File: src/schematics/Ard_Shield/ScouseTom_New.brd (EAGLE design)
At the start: 129.7 x 53.7 mm, 64 parts, among them IC1 LM317MBDT, IC2 AD5280, J1 STIM OUT, J4 Stim out Brd, Q2 FDN304P, Q3 FDV303N, T1 BC817, U1 ADM3202ARUZ, U3 ADUM5402ARWZ, U4 ADUM1410ARWZ, U5 ADUM5000ARWZ, U7 ADUM1410ARWZ, X1 IND DSUB, X2 SW DSUB, X3 CS DSUB

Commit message: gerber files and ignoring eagle backups
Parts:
- moved JP1 1.50 mm to (2.21, 38.1)
- moved J1 0.50 mm to (99.9, 16.6)
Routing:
- net GND_ISO_RS232: track 101.7 -> 99.7 mm, vias 9 -> 20
- net CS_EXTRA_ISO: track 32.9 -> 31.4 mm
- net STIM_OUT: track 23.5 -> 24.0 mm
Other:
- board text added: "???"
- board text added: "BONUS PINS"
- board text added: "CS Extra"
- board text added: "PMRK"
- board text added: "Tst1"
- board text added: "Tst2"
- board text added: "UCL EIT SCOUSETOM V2.5"
- board text removed: "PMARK"
- board text removed: "UCL EIT SCOUSETOM V2"

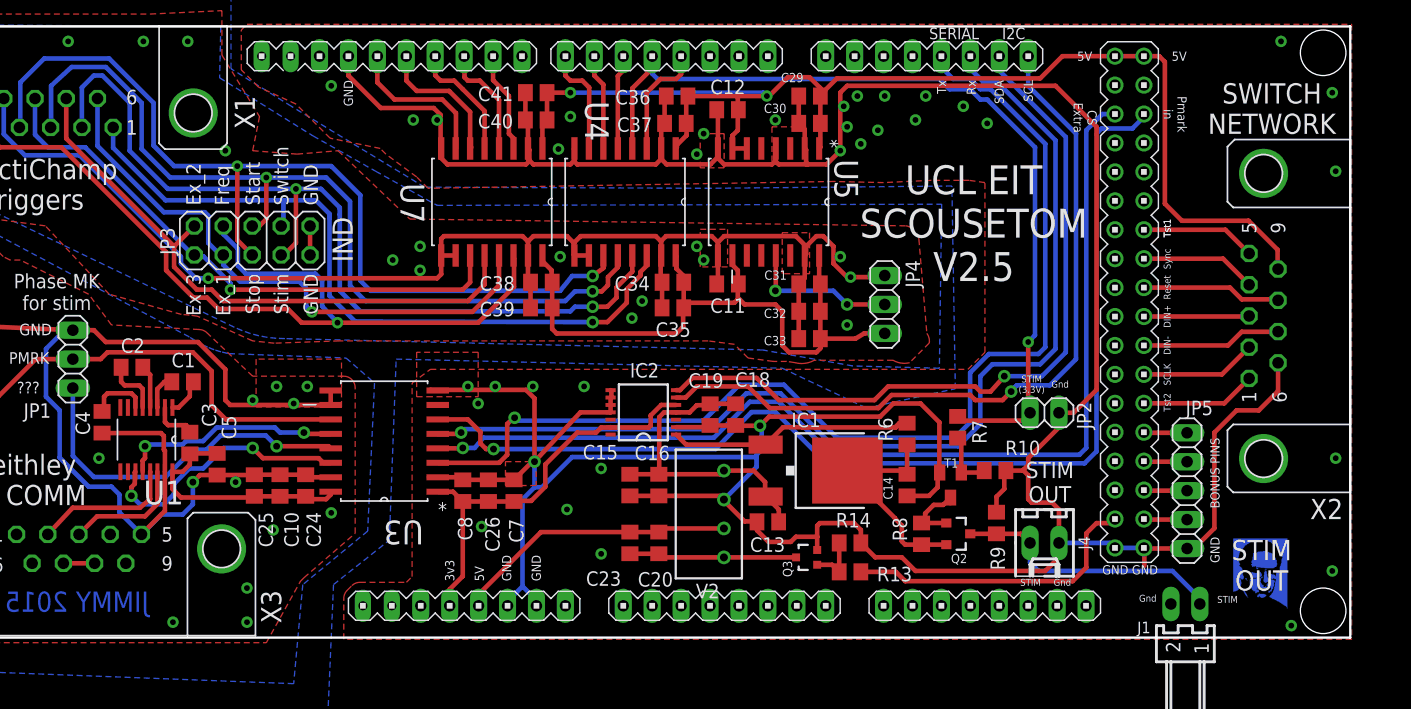
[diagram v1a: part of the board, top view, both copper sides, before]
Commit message: Final version sent to PCBTrain with BOM and P&P
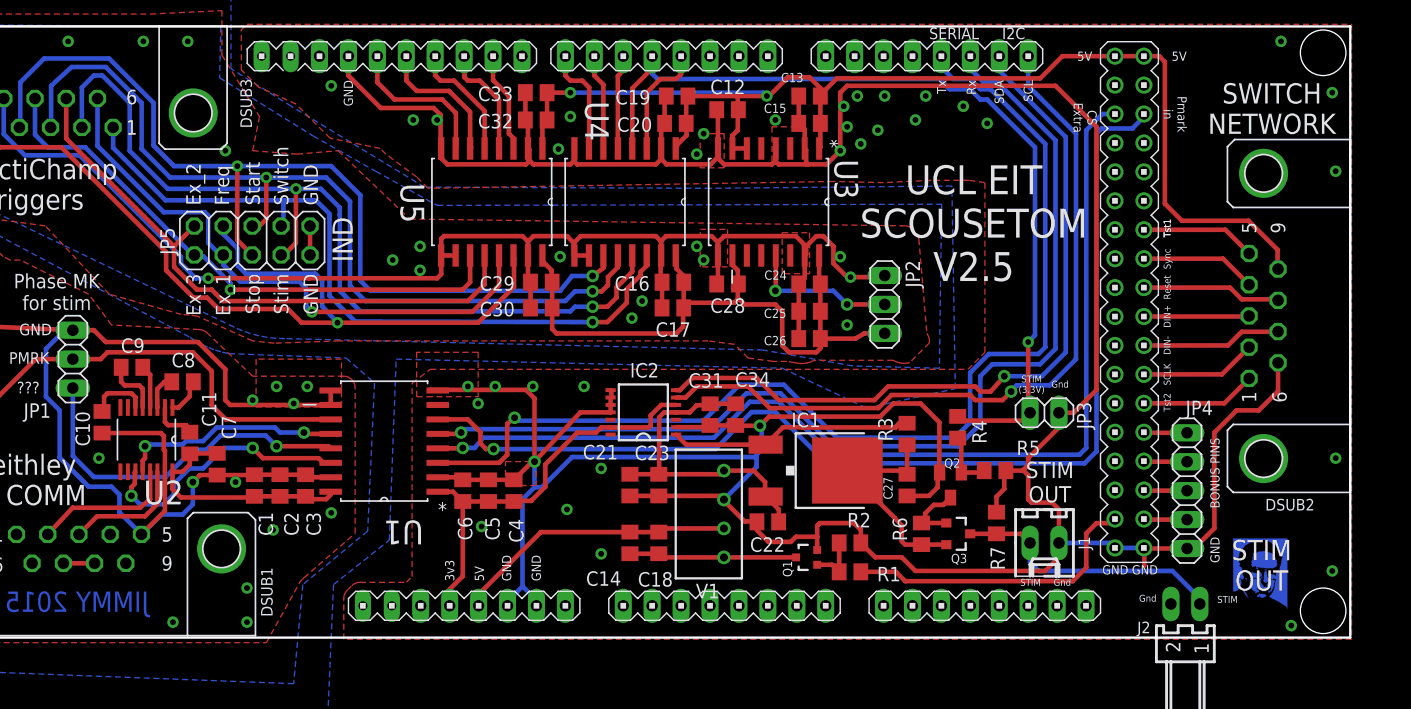
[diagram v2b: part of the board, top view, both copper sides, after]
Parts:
- removed C36, C38, C40: .1uF, resistor:C0805
- removed C37, C39, C41: 1uF, resistor:C0805
- removed J4: Stim out Brd, con-molex:6410-02
- removed R8: 5K1, resistor:R0805
- removed R9: 3k, resistor:R0805
- removed T1: BC817, transistor-npn:SOT23-BEC
- removed U7: ADUM1410ARWZ, ADI-Phase-2:SOIC127P1032X265-16N
- added C21, C28, C6: 10uF, resistor:C0805
- added C22, C9: 0.1uF, resistor:C0805
- added C27: 1uF, resistor:C0805
- added J2: STIM OUT, con-molex:7395-02
- added Q1: FDV303N, SparkFun-DiscreteSemi:SOT323
- added R3: 470, resistor:R0805
- added R4: 33k, resistor:R0805
- added U2: ADM3202ARUZ, Analog Devices_By_element14_Batch_1:SOP65P640X120-16N
- C1, C4: value 0.1uF -> 10nF
- C10, C34: value .1uF -> 0.1uF
- C11, C23, C8: value 10uF -> 0.1uF
- C13, C16, C2, C5: value 0.1uF -> .1uF
- C14: value 1uF -> 10uF
- C19: value 10uF -> .1uF
- C20: value 0.1uF -> 1uF
- C25: value 10nF -> .1uF
- C26: value .1uF -> 10nF
- C3: value 0.1uF -> 10uF
- C30: value 10uF -> 1uF
- C33: value 10nF -> 1uF
- C7: value 10nF -> 0.1uF
- J1: value STIM OUT -> Stim out Brd; device con-molex:7395-02 -> con-molex:6410-02
- JP2: value Ext Stim -> V_TRIG_SELECT; device pinhead:1X02 -> pinhead:1X03
- JP3: value IND_BK -> Ext Stim; device pinhead:2X05 -> pinhead:1X02
- JP4: value V_TRIG_SELECT -> BONUS_PINOUT; device pinhead:1X03 -> pinhead:1X05
- JP5: value BONUS_PINOUT -> IND_BK; device pinhead:1X05 -> pinhead:2X05
- Q2: value FDN304P -> BC817; device SparkFun-DiscreteSemi:SOT23-3 -> transistor-npn:SOT23-BEC
- Q3: value FDV303N -> FDN304P; device SparkFun-DiscreteSemi:SOT323 -> SparkFun-DiscreteSemi:SOT23-3
- R6: value 470 -> 5K1
- R7: value 33k -> 3k
- U1: value ADM3202ARUZ -> ADUM5402ARWZ; device Analog Devices_By_element14_Batch_1:SOP65P640X120-16N -> Analog Devices_By_element14_Batch_1:SOIC127P1032X265-16N
- U3: value ADUM5402ARWZ -> ADUM5000ARWZ
- U5: value ADUM5000ARWZ -> ADUM1410ARWZ; device Analog Devices_By_element14_Batch_1:SOIC127P1032X265-16N -> ADI-Phase-2:SOIC127P1032X265-16N
- moved JP5 85.0 mm to (18.0, 48.5), turned to 0 degrees
- moved JP3 71.2 mm to (87.5, 33.4)
- moved C25 51.1 mm to (66.9, 42.3), turned to 180 degrees
- moved C11 49.2 mm to (12.5, 30.7), turned to 90 degrees
- moved C24 47.7 mm to (66.9, 44.7), turned to 180 degrees
- moved U3 39.8 mm to (63.3, 51.9), turned to 270 degrees
- moved C13 37.6 mm to (66.9, 61.2), turned to 180 degrees
- moved C20 36.9 mm to (55.1, 58.8), turned to 180 degrees
- moved C4 36.7 mm to (41.0, 26.6), turned to 90 degrees
- moved C15 35.5 mm to (66.9, 58.8), turned to 180 degrees
- moved C33 32.3 mm to (42.9, 61.5)
- moved C26 31.2 mm to (66.9, 39.9), turned to 180 degrees
- moved JP4 31.2 mm to (100.0, 26.6)
- moved C32 29.3 mm to (42.9, 59.1)
- moved C29 28.7 mm to (43.4, 44.9)
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- renumbered C35 to C17, DIN8 to DIN1, DUE to ARD1, R10 to R5, R13 to R1, R14 to R2, V2 to V1, X1 to DSUB3, X2 to DSUB2, X3 to DSUB1
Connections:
- net +3V3: now also C4.1, C5.1, C6.1, U1.1; no longer C26.1, C7.1, C8.1, U3.1
- net +5V: now also C13.1, C15.1, C19.1, C20.1, C32.1, C33.1, U3.1, U3.6, U3.7; no longer C29.1, C30.1, C36.1, C37.1, C40.1, C41.1, U5.6, U5.7, U7.1
- net 5V_SIDE: now also C14.1, C18.2; no longer C20.2, C23.1
- net BONUS_1: now also JP4.1; no longer JP5.1
- net BONUS_2: now also JP4.2; no longer JP5.2
- net BONUS_3: now also JP4.3; no longer JP5.3
- net BONUS_4: now also JP4.4; no longer JP5.4
- net CS_EXTRA: now also U1.4; no longer U3.4
- net CS_EXTRA_ISO: now also U1.13; no longer U3.13
- net CS_PMARK: now also U1.6; no longer U3.6
- net CS_PMARK_ISO: now also U1.11; no longer U3.11
- net GND: now also C13.2, C20.2, C21.2, C22.1, C23.1, C27.1, C31.2, C32.2, C33.2, C34.1, C4.2, C5.2, C6.2, J2.2, JP3.2, JP4.5, Q1.2, Q2.E, R7.1, U1.2, U1.8, U3.3, U3.4; no longer C13.1, C14.1, C16.1, C18.1, C26.2, C29.2, C30.2, C36.2, C37.2, C40.2, C41.2, C7.2, C8.2, J4.2, JP2.2, JP5.5, Q3.2, R9.1, T1.E, U5.3, U5.4, U7.2, U7.8
- net GND_ISO_RS232: now also C1.2, C2.2, C3.2, C7.2, U1.10, U1.9, U2.15; no longer C24.2, C25.2, C4.2, C5.2, U3.10, U3.15, U3.9
- net GND_ISO_TRIG: now also C16.2, C24.2, C25.2, C26.2, C28.2, C29.2, C30.2, JP2.1, JP5.10, JP5.9, U3.11, U3.12, U3.14, U3.15, U3.9, U5.10; no longer C11.2, C31.2, C32.2, C33.2, C34.2, C38.2, C39.2, JP3.10, JP3.9, JP4.1, U5.11, U5.12, U5.14, U7.10, U7.15, U7.9
- net IND_EX_1: now also U5.4; no longer U7.4
- net IND_EX_1_ISO: now also JP5.3, U5.13; no longer JP3.3, U7.13
- net IND_EX_2: now also U5.5; no longer U7.5
- net IND_EX_2_ISO: now also JP5.2, U5.12; no longer JP3.2, U7.12
- net IND_EX_3: now also U5.6; no longer U7.6
- net IND_EX_3_ISO: now also JP5.1, U5.11; no longer JP3.1, U7.11
- net IND_FREQ: now also U5.3; no longer U7.3
- net IND_FREQ_ISO: now also JP5.4, U5.14; no longer JP3.4, U7.14
- net IND_START_ISO: now also JP5.6; no longer JP3.6
- net IND_STIM: now also JP3.1, R4.1; no longer JP2.1, R7.1
- net IND_STIM_ISO: now also JP5.7; no longer JP3.7
- net IND_STOP_ISO: now also JP5.5; no longer JP3.5
- net IND_SWITCH_ISO: now also JP5.8; no longer JP3.8
- net N$1: now also Q2.B, R4.2; no longer R7.2, T1.B
- net N$22: now also C8.2, U2.1; no longer C1.2, U1.1
- net N$23: now also C8.1, U2.3; no longer C1.1, U1.3
- net N$24: now also C9.2, U2.4; no longer C2.2, U1.4
- net N$25: now also C9.1, U2.5; no longer C2.1, U1.5
- net N$26: now also C11.2, U2.2; no longer C3.2, U1.2
- net N$27: now also C10.1, U2.6; no longer C4.1, U1.6
- net N$3: now also Q2.C, Q3.1, R6.2; no longer Q2.1, R8.2, T1.C
- net N$5: now also Q1.1; no longer Q3.1
- net POT_IN: now also R3.2; no longer R6.2
- net RS232_RXD: now also U2.14; no longer U1.14
- net RS232_TXD: now also U2.13; no longer U1.13
- net STIM_OUT: now also J2.1, Q3.3, R7.2; no longer J4.1, Q2.3, R9.2
- net STIM_REG_VIN-: now also C14.2, C18.1, Q1.3; no longer C20.1, C23.2, Q3.3
- net TRIG_DISABLE_2: now also U5.7; no longer U7.7
- net TTL_RX: now also U1.5; no longer U3.5
- net TTL_RX_ISO: now also U2.12; no longer U3.12
- net TTL_TX: now also U1.3; no longer U3.3
- net TTL_TX_ISO: now also U1.14, U2.11; no longer U1.11, U3.14
- net V_ISO_RS232: now also C1.1, C11.1, C2.1, C7.1, U2.16; no longer C10.1, C24.1, C25.1, C5.1, U3.16
- net V_ISO_TRIG: now also C16.1, C24.1, C25.1, C26.1, C28.1, C29.1, C30.1, JP2.3, U3.10, U3.16; no longer C11.1, C31.1, C32.1, C33.1, C34.1, C38.1, C39.1, JP4.3, U5.10, U7.16
- net V_SELECT: now also JP2.2, U3.13; no longer JP4.2, U5.13
- net V_STIM: now also C27.2, Q3.2, R3.1; no longer C14.2, Q2.2, R8.1
- net V_STIM_REF: now also C21.1, C22.2, C23.2, C31.1, C34.2; no longer C13.2, C15.1, C16.2, C18.2, C19.1
